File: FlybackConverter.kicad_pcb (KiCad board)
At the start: 2 copper layers, 76.2 x 76.2 mm, 46 parts, among them J1 USB_C_Receptacle_PowerOnly_6P, T1 Transformer_1P_2S, U1 LNK6428K, U2 TPS25820DSST

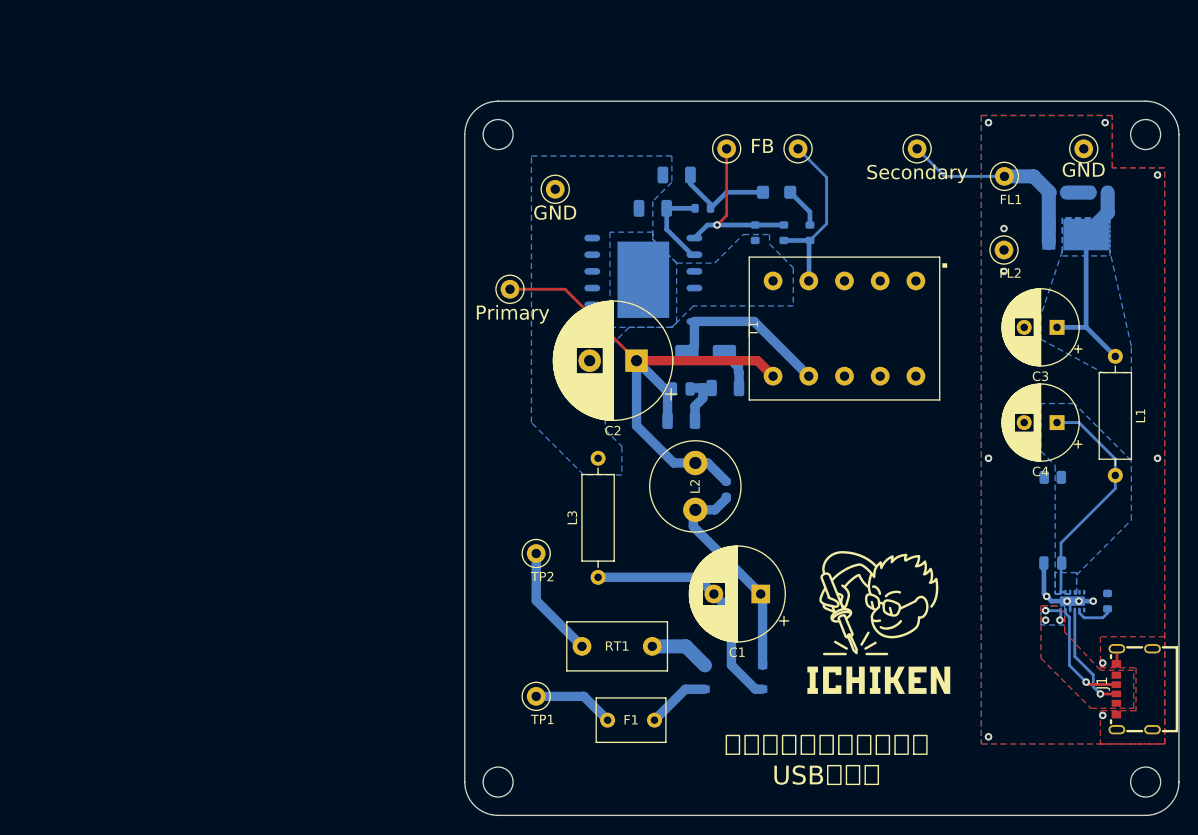
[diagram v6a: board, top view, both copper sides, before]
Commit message: TP以外大体配置できた #10
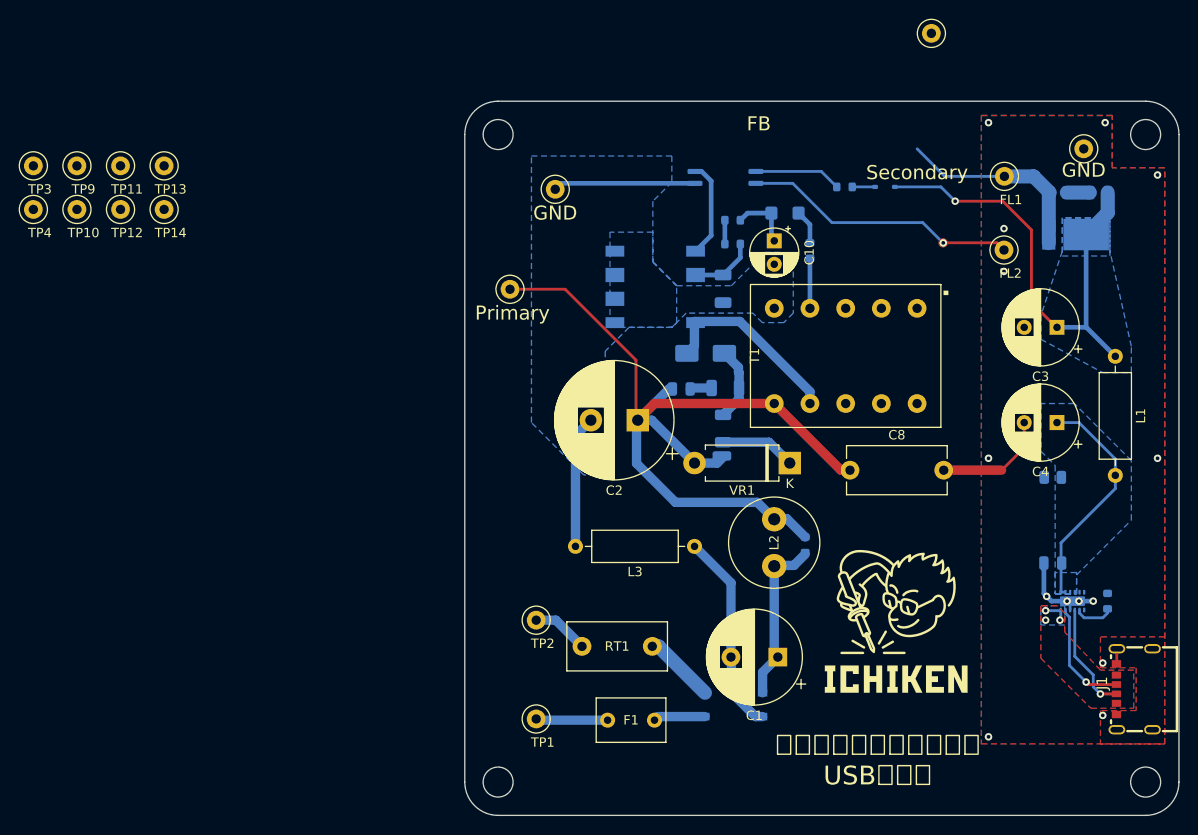
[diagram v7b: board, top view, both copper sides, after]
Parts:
- added C10: 33u, Capacitor_THT:CP_Radial_D5.0mm_P2.50mm, F.Cu at (160.0, 65.7)
- added D4: 3.9V, Diode_SMD:D_SOD-323, B.Cu at (171.8, 59.9)
- added REF**: SolderWirePad_1x01_SMD_1x2mm, Connector_Wire:SolderWirePad_1x01_SMD_1x2mm, B.Cu at (154.4, 88.6)
- added TP10: 5V, TestPoint:TestPoint_Loop_D1.80mm_Drill1.0mm_Beaded, F.Cu at (85.6, 62.3)
- added TP11: EN/UV, TestPoint:TestPoint_Loop_D1.80mm_Drill1.0mm_Beaded, F.Cu at (90.3, 57.7)
- added TP12: BP, TestPoint:TestPoint_Loop_D1.80mm_Drill1.0mm_Beaded, F.Cu at (90.3, 62.3)
- added TP13: GND, TestPoint:TestPoint_Loop_D1.80mm_Drill1.0mm_Beaded, F.Cu at (94.9, 57.7)
- added TP14: GND, TestPoint:TestPoint_Loop_D1.80mm_Drill1.0mm_Beaded, F.Cu at (94.9, 62.3)
- added TP9: DRAIN, TestPoint:TestPoint_Loop_D1.80mm_Drill1.0mm_Beaded, F.Cu at (85.6, 57.7)
- added U3: TLP291, Package_SO:SOIC-4_4.55x2.6mm_P1.27mm, B.Cu at (154.8, 58.9)
- added VR1: P6KE150A, Diode_THT:D_DO-15_P10.16mm_Horizontal, F.Cu at (161.7, 89.4)
- C6: value 470p -> 10nF
- C7: value 1u -> 100n
- C8: value 10u -> 2.2n; footprint Capacitor_SMD:C_1206_3216Metric -> Capacitor_THT:C_Disc_D10.5mm_W5.0mm_P10.00mm; moved to F.Cu
- R11: value 200k -> 1k
- R3: value 150 -> 100
- R5: value 2.4 -> 47
- R6: value 42.2 -> 1
- R7: value 10k -> 390
- R8: value 2.37k -> 8.06k
- TP3: value TestPoint -> BP/M
- TP4: value TestPoint -> EN
- U1: value LNK6428K -> TNY278G; footprint Package_SO:PowerIntegrations_eSOP-12B -> Package_DIP:PowerIntegrations_SMD-8C
- moved TP3 81.6 mm to (81.0, 57.7)
- moved TP4 74.3 mm to (81.0, 62.3)
- moved C8 36.5 mm to (168.1, 90.2), turned to 0 degrees
- moved TP5 12.4 mm to (176.8, 43.6)
- moved C7 11.4 mm to (154.6, 70.8), turned to -90 degrees
- moved L3 10.8 mm to (151.5, 98.3), turned to 180 degrees
- moved R7 10.7 mm to (167.5, 59.9), turned to 180 degrees
- moved L2 10.3 mm to (160.0, 100.4)
- moved R10 10.3 mm to (163.3, 98.1)
- moved R5 8.36 mm to (155.6, 63.5), turned to 180 degrees
- moved TP2 7.11 mm to (134.6, 106.2)
- moved C1 6.97 mm to (160.4, 110.1)
- moved C2 6.35 mm to (145.5, 84.8)
- moved R8 4.96 mm to (155.6, 66.0)
- moved R11 4.53 mm to (154.6, 85.7), turned to 90 degrees
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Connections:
- net Net-(D1-K) renamed EN
- C2 pad 2: Net-(T1-SB) -> Net-(T1-SA)
- C7 pad 1: Net-(U1-BP) -> Net-(U1-BP/M)
- C7 pad 2: Net-(T1-SB) -> Net-(T1-SA)
- C8 pad 1: Net-(D3-K) -> PRI
- C8 pad 2: Net-(T1-SB) -> FL2
- D2 pad 2: Net-(D2-A) -> DRAIN
- L3 pad 2: Net-(T1-SB) -> Net-(T1-SA)
- R11 pad 1: PRI -> Net-(VR1-K)
- R11 pad 2: Net-(C6-Pad2) -> Net-(D2-K)
- R5 pad 1: FB -> Net-(D3-K)
- R5 pad 2: Net-(D3-A) -> Net-(R5-Pad2)
- R6 pad 1: FB -> Net-(T1-SB)
- R6 pad 2: Net-(U1-FB) -> Net-(D3-A)
- R7 pad 1: Net-(U1-FB) -> Net-(D4-A)
- R7 pad 2: Net-(T1-SB) -> Net-(R7-Pad2)
- R8 pad 1: Net-(U1-BP) -> Net-(R5-Pad2)
- R8 pad 2: Net-(D3-K) -> Net-(U1-BP/M)
- T1 pad 4: FB -> Net-(T1-SB)
- T1 pad 5: Net-(T1-SB) -> Net-(T1-SA)
- T1 pad 7: Net-(D2-A) -> DRAIN
- TP3 pad 1: FB -> Net-(U1-BP/M)
- TP4 pad 1: Net-(U1-FB) -> Net-(D4-A)
- TP8 pad 1: Net-(T1-SB) -> Net-(T1-SA)
- U1 pad 1: Net-(U1-FB) -> Net-(U1-EN/UV)
- U1 pad 2: Net-(U1-BP) -> Net-(U1-BP/M)
- U1 pad 4: Net-(T1-SB) -> DRAIN
- U1 pad 6: Net-(D2-A) -> Net-(T1-SA)
- U1 pad 7: Net-(T1-SB) -> Net-(T1-SA)
- U1 pad 8: Net-(T1-SB) -> Net-(T1-SA)
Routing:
- net FL2: track 11.1 -> 52.7 mm, vias 14 -> 15
- net PRI: track 59.8 -> 91.7 mm
- net Net-(T1-SA): track 0.00 -> 29.3 mm
- net EN: track 22.8 -> 50.9 mm, vias 0 -> 1
- net DRAIN: track 0.00 -> 20.4 mm
- net FB: track 18.9 -> 0.00 mm
- net Net-(U1-FB): track 18.7 -> 0.00 mm, vias 1 -> 0
- net Net-(D2-A): track 18.4 -> 0.00 mm
- net Net-(U1-EN/UV): track 0.00 -> 10.3 mm
- net Net-(U1-BP): track 9.36 -> 0.00 mm
- net Net-(R7-Pad2): track 0.00 -> 9.31 mm
- net Net-(VR1-K): track 0.00 -> 8.03 mm
- net Net-(U1-BP/M): track 0.00 -> 7.00 mm
- net Net-(RT1-Pad2): track 11.9 -> 6.04 mm
- net Net-(BR1-+): track 23.8 -> 18.1 mm
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
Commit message: TP配置
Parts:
- added TP15: GND, TestPoint:TestPoint_Loop_D1.80mm_Drill1.0mm_Beaded, F.Cu at (199.6, 101.3)
- TP1, TP2: value TestPoint -> AC IN
- TP5: value TestPoint -> SEC
- TP6: value TestPoint -> GND
- TP7: value Primary -> PRI
- moved TP10 114.4 mm to (194.9, 95.9)
- moved TP4 88.4 mm to (169.0, 54.2)
- moved TP3 71.1 mm to (152.0, 54.2)
- moved TP12 69.6 mm to (159.4, 54.2)
- moved TP11 54.0 mm to (144.1, 54.2)
- moved TP13 51.3 mm to (135.6, 88.9)
- moved TP9 48.2 mm to (132.0, 70.9)
- moved TP14 41.8 mm to (136.7, 59.6)
- moved TP5 10.7 mm to (178.1, 54.2)
- moved TP7 9.91 mm to (131.8, 80.8)
- moved TP8 5.21 mm to (136.7, 65.4)
- moved R7 4.85 mm to (170.9, 63.4)
- moved D4 4.76 mm to (175.1, 63.4)
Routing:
- net DRAIN: track 20.4 -> 41.9 mm, vias 0 -> 1
- net Net-(T1-SB): track 5.33 -> 21.8 mm, vias 0 -> 1
- net Net-(U1-BP/M): track 7.00 -> 22.1 mm, vias 0 -> 1
- net Net-(D4-A): track 2.44 -> 12.6 mm
- net Net-(U1-EN/UV): track 10.3 -> 18.5 mm
- net PRI: track 91.7 -> 83.9 mm
- net EN: track 50.9 -> 43.2 mm
- net Net-(R7-Pad2): track 9.31 -> 14.2 mm
- net FL1: track 21.4 -> 19.7 mm
- net FL2: vias 15 -> 14
- added copper zone on B.Cu, net Net-(T1-SA)
- removed copper zone on B.Cu, net Net-(T1-SB)
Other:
- board text removed: "FB"
- board text removed: "GND"
- board text removed: "Primary"
- board text removed: "Secondary"
